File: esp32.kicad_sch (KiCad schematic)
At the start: 10 parts, among them U1 ESP32-C3-WROOM-02

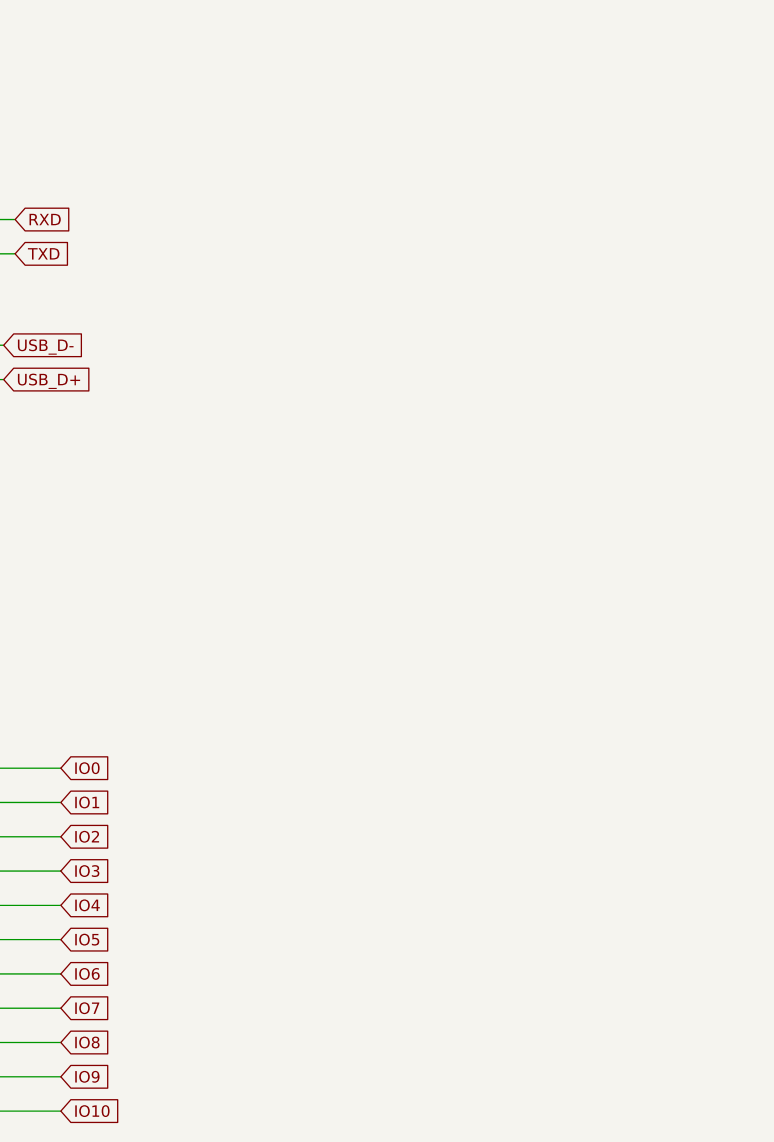
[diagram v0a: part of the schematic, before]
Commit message: Rework v4 schematic for Raspberry Pi 4/5 HAT
- Remap J1 to the Raspberry Pi 40-pin pinout (was still Orange Pi pin
  numbers: Pi 3V3 on MISO, GND on ESP32 RX)
- Fix auto-reset: U4 collectors drove EN and IO9 the wrong way round
- Let the Pi flash the ESP32: UART via 74LVC1G08 AND gate (U10) shared
  with the CP2102N, EN/BOOT on GPIO5/6 through 1k; add IO9 pull-up
- Power the Pi straight from +5V, drop the SS34 diode (D6)
- Add fan control: AO3400A low-side switch on GPIO18, tach on GPIO24
- Move mux LEDs D1-D3 off strapping pin GPIO8 to the 5V select lines
- Add 3V3 power LED and test points TP8-TP33
- Document v4 in CLAUDE.md

Co-Authored-By: Claude Opus 5.5 <noreply@anthropic.com>
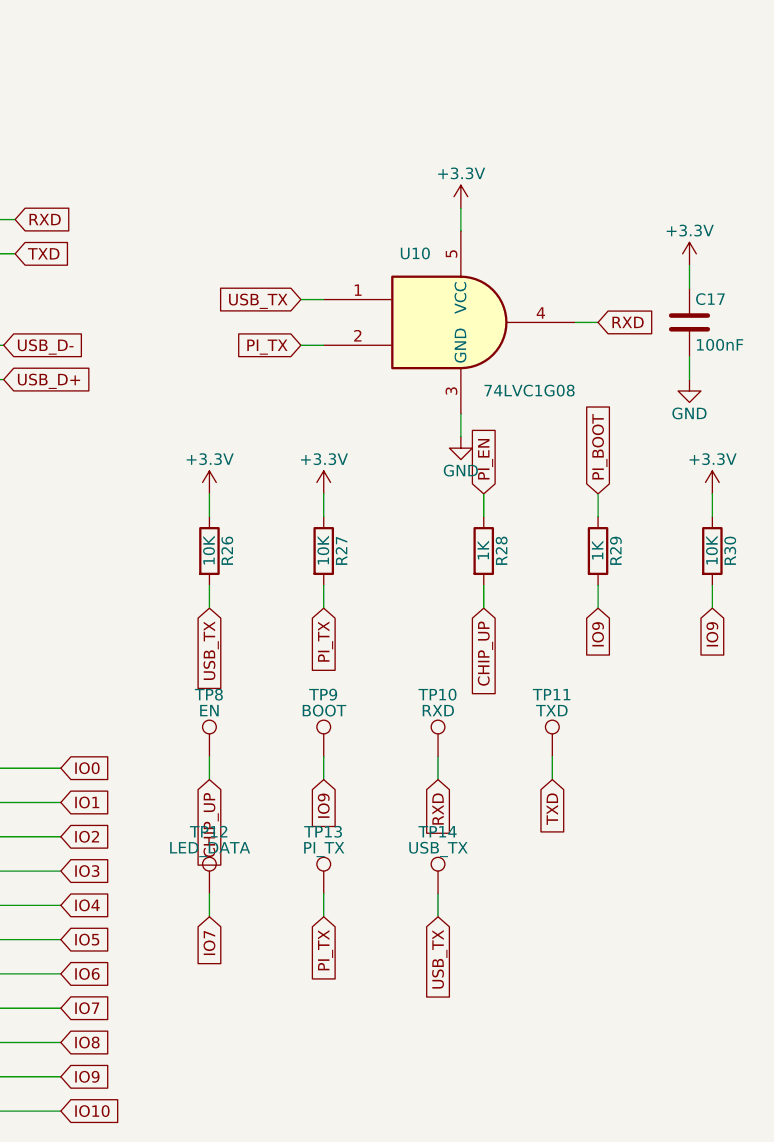
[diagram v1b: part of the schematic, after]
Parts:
- added C17: 100nF, Capacitor_SMD:C_0603_1608Metric, symbol Device:C
- added R26, R27, R30: 10K, Resistor_SMD:R_0603_1608Metric, symbol Device:R
- added R28, R29: 1K, Resistor_SMD:R_0603_1608Metric, symbol Device:R
- added TP10: RXD, TestPoint:TestPoint_Pad_1.0x1.0mm, symbol Connector:TestPoint
- added TP11: TXD, TestPoint:TestPoint_Pad_1.0x1.0mm, symbol Connector:TestPoint
- added TP12: LED_DATA, TestPoint:TestPoint_Pad_1.0x1.0mm, symbol Connector:TestPoint
- added TP13: PI_TX, TestPoint:TestPoint_Pad_1.0x1.0mm, symbol Connector:TestPoint
- added TP14: USB_TX, TestPoint:TestPoint_Pad_1.0x1.0mm, symbol Connector:TestPoint
- added TP8: EN, TestPoint:TestPoint_Pad_1.0x1.0mm, symbol Connector:TestPoint
- added TP9: BOOT, TestPoint:TestPoint_Pad_1.0x1.0mm, symbol Connector:TestPoint
- added U10: 74LVC1G08, Package_TO_SOT_SMD:SOT-353_SC-70-5, symbol 74xGxx:74LVC1G08
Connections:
- net +3.3V: now also C17.1, R26.1, R27.1, R30.1, U10.5 (VCC)
- net CHIP_UP: now also R28.2, TP8.1
- net GND: now also C17.2, U10.3 (GND)
- net IO7: now also TP12.1
- net IO9: now also R29.2, R30.2, TP9.1
- net RXD: now also TP10.1, U10.4
- net TXD: now also TP11.1
- new net PI_BOOT: R29.1
- new net PI_EN: R28.1
- new net PI_TX: R27.2, TP13.1, U10.2
- new net USB_TX: R26.2, TP14.1, U10.1

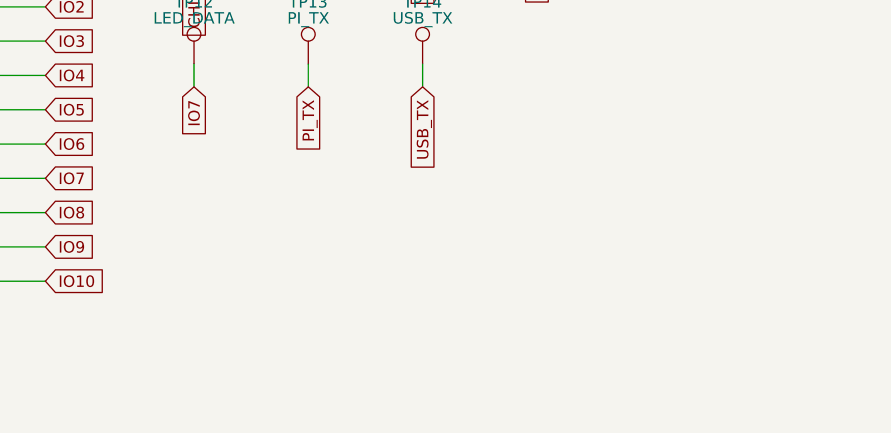
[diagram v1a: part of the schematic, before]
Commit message: Apply schematic review fixes, add JLCPCB rules, prepare for manual layout
Schematic (from a Codex review):
- R35 10k pull-up on GPIO2 (strapping pin; Pi MISO has a default pull-down)
- R36 10k pull-down on IO7 so the LEDs stay dark while the ESP32 boots
- C5 22uF for AMS1117 output stability, C7 1nF on GPIO9
- C18-C21 100nF decoupling for the level shifters U6-U9

Board:
- New parts parked outside the outline for manual placement
- Silkscreen scaled to JLCPCB's 1.0 mm minimum; back pinout table rebuilt
- C5/C7 values synced

Rules:
- JLCPCB 4-layer limits in Julelys.kicad_pro and new Julelys.kicad_dru

Co-Authored-By: Claude Opus 5.5 <noreply@anthropic.com>
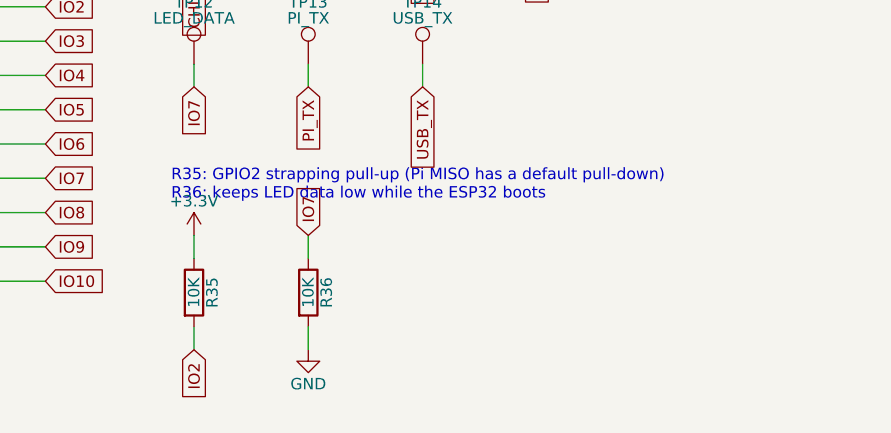
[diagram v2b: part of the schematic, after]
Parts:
- added R35, R36: 10K, Resistor_SMD:R_0603_1608Metric, symbol Device:R
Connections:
- net +3.3V: now also R35.1
- net GND: now also R36.2
- net IO2: now also R35.2
- net IO7: now also R36.1
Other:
- note added: "R35: GPIO2 strapping pull-up (Pi MISO has a default pull-down) R36: keeps LED data low while the ESP32 boots"
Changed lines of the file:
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@@
     )
   )
+  (symbol (lib_id "Device:R") (at 200.66 152.4 0) (unit 1)
+    (in_bom yes) (on_board yes) (dnp no)
+    (property "Reference" "R35" (at 202.692 152.4 90)
+      (effects (font (size 1.27 1.27)))
+    )
+    (property "Value" "10K" (at 200.66 152.4 90)
+      (effects (font (size 1.27 1.27)))
+    )
+    (property "Footprint" "Resistor_SMD:R_0603_1608Metric" (at 198.882 152.4 90)
+      (effects (font (size 1.27 1.27)) hide)
+    )
+    (property "Datasheet" "~" (at 200.66 152.4 0)
+      (effects (font (size 1.27 1.27)) hide)
+    )
+    (pin "1")
+    (pin "2")
+    (instances
+      (project "Julelys"
+        (path "/9ef41b73-8dcb-4021-8930-5b1db22eb182/9665c677-0b50-4f2a-bdc6-f5e1c3cc96ed"
+          (reference "R35") (unit 1)
+        )
+      )
+    )
+  )
+  (wire (pts (xy 200.66 148.59) (xy 200.66 146.05))
+    (stroke (width 0) (type default))
+  )
+  (symbol (lib_id "power:+3.3V") (at 200.66 146.05 0) (unit 1)
+    (in_bom yes) (on_board yes) (dnp no) (fields_autoplaced)
+    (property "Reference" "#PWR0201" (at 200.66 146.05 0)
+      (effects (font (size 1.27 1.27)) hide)
+    )
+    (property "Value" "+3.3V" (at 200.66 142.24 0)
+      (effects (font (size 1.27 1.27)))
+    )
+    (property "Footprint" "" (at 200.66 146.05 0)
+      (effects (font (size 1.27 1.27)) hide)
+    )
+    (property "Datasheet" "" (at 200.66 146.05 0)
+      (effects (font (size 1.27 1.27)) hide)
+    )
+    (pin "1")
+    (instances
+      (project "Julelys"
+        (path "/9ef41b73-8dcb-4021-8930-5b1db22eb182/9665c677-0b50-4f2a-bdc6-f5e1c3cc96ed"
+          (reference "#PWR0201") (unit 1)
+        )
+      )
+    )
+  )
+  (wire (pts (xy 200.66 156.21) (xy 200.66 158.75))
+    (stroke (width 0) (type default))
+  )
+  (global_label "IO2" (shape input) (at 200.66 158.75 270) (fields_autoplaced)
+    (effects (font (size 1.27 1.27)) (justify right))
+    (property "Intersheetrefs" "${INTERSHEET_REFS}" (at 200.66 158.75 270)
+      (effects (font (size 1.27 1.27)) (justify right) hide)
+    )
+  )
+  (symbol (lib_id "Device:R") (at 213.36 152.4 0) (unit 1)
+    (in_bom yes) (on_board yes) (dnp no)
+    (property "Reference" "R36" (at 215.392 152.4 90)
+      (effects (font (size 1.27 1.27)))
+    )
+    (property "Value" "10K" (at 213.36 152.4 90)
+      (effects (font (size 1.27 1.27)))
+    )
+    (property "Footprint" "Resistor_SMD:R_0603_1608Metric" (at 211.582 152.4 90)
+      (effects (font (size 1.27 1.27)) hide)
+    )
+    (property "Datasheet" "~" (at 213.36 152.4 0)
+      (effects (font (size 1.27 1.27)) hide)
+    )
+    (pin "1")
+    (pin "2")
+    (instances
+      (project "Julelys"
+        (path "/9ef41b73-8dcb-4021-8930-5b1db22eb182/9665c677-0b50-4f2a-bdc6-f5e1c3cc96ed"
+          (reference "R36") (unit 1)
+        )
+      )
+    )
+  )
+  (wire (pts (xy 213.36 148.59) (xy 213.36 146.05))
+    (stroke (width 0) (type default))
+  )
+  (global_label "IO7" (shape input) (at 213.36 146.05 90) (fields_autoplaced)
+    (effects (font (size 1.27 1.27)) (justify left))
+    (property "Intersheetrefs" "${INTERSHEET_REFS}" (at 213.36 146.05 90)
+      (effects (font (size 1.27 1.27)) (justify left) hide)
+    )
+  )
+  (wire (pts (xy 213.36 156.21) (xy 213.36 158.75))
+    (stroke (width 0) (type default))
+  )
+  (symbol (lib_id "power:GND") (at 213.36 158.75 0) (unit 1)
+    (in_bom yes) (on_board yes) (dnp no) (fields_autoplaced)
+    (property "Reference" "#PWR0202" (at 213.36 158.75 0)
+      (effects (font (size 1.27 1.27)) hide)
+    )
+    (property "Value" "GND" (at 213.36 162.56 0)
+      (effects (font (size 1.27 1.27)))
+    )
+    (property "Footprint" "" (at 213.36 158.75 0)
+      (effects (font (size 1.27 1.27)) hide)
+    )
+    (property "Datasheet" "" (at 213.36 158.75 0)
+      (effects (font (size 1.27 1.27)) hide)
+    )
+    (pin "1")
+    (instances
+      (project "Julelys"
+        (path "/9ef41b73-8dcb-4021-8930-5b1db22eb182/9665c677-0b50-4f2a-bdc6-f5e1c3cc96ed"
+          (reference "#PWR0202") (unit 1)
+        )
+      )
+    )
+  )
+  (text "R35: GPIO2 strapping pull-up (Pi MISO has a default pull-down)\nR36: keeps LED data low while the ESP32 boots" (at 198.12 142.24 0)
+    (effects (font (size 1.27 1.27)) (justify left bottom))
+  )
 )

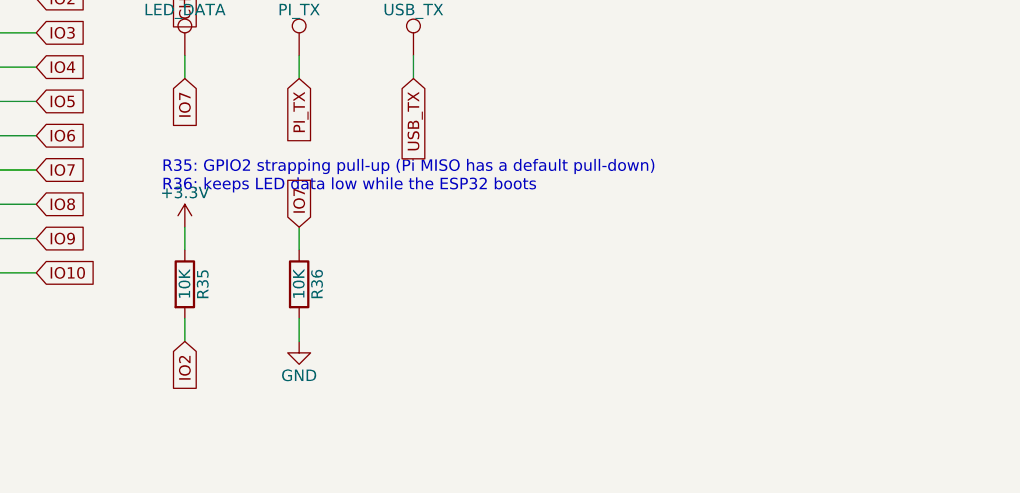
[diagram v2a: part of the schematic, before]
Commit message: Place decoupling caps, remove fan circuit and J3, add spare ESP32-Pi lines
Schematic:
- Remove the fan circuit (J13, Q1, D8, R31-R33, TP15-17); the Pi 5 drives
  its own Active Cooler. J1 pins 12/18 are now no-connect
- Remove the J3 debug header; J1 doubles as the dev header without a Pi
- IO0/IO1 to J1 pins 37/36 (Pi GPIO26/16) through R37/R38 1k as spare lines

Board:
- Test points moved to the bottom side to free space on top
- Decoupling caps C2/C3/C5/C8/C16/C18-C21 and R35/R36 placed next to
  their ICs; U8 nudged and R23/R10 moved to make room
- Conflicting tracks ripped up and rerouted; 6 connections left for
  interactive routing
- Back pinout table updated (fan and J3 rows replaced by J1 37/36)
- Courtyard exception rule for caps inside their IC's courtyard margin
- DRC (JLCPCB rules): 0 errors; ERC: 0 errors; schematic parity clean

Co-Authored-By: Claude Opus 5.5 <noreply@anthropic.com>
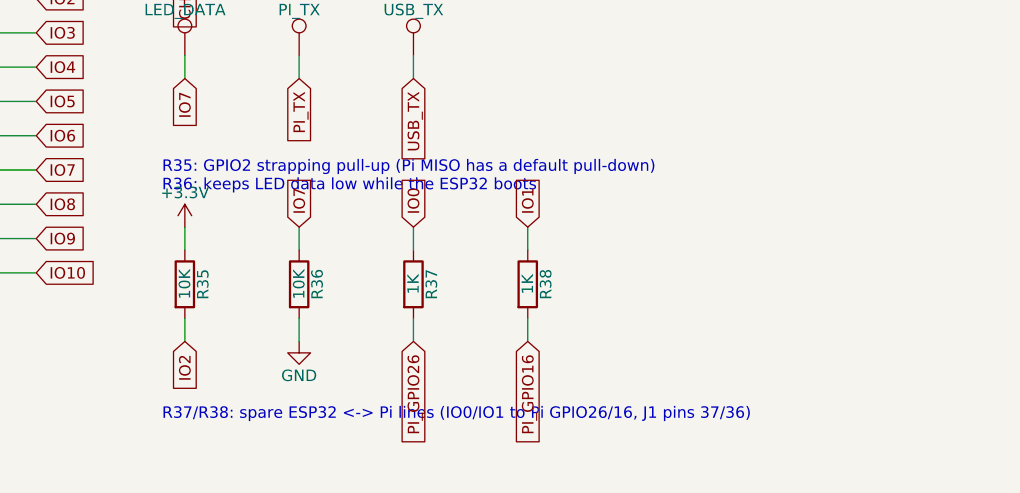
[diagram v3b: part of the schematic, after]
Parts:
- added R37, R38: 1K, Resistor_SMD:R_0603_1608Metric, symbol Device:R
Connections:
- net IO0: now also R37.1
- net IO1: now also R38.1
- new net PI_GPIO16: R38.2
- new net PI_GPIO26: R37.2
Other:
- note added: "R37/R38: spare ESP32 <-> Pi lines (IO0/IO1 to Pi GPIO26/16, J1 pins 37/36)"
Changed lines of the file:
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@@
+    (effects (font (size 1.27 1.27)) (justify left bottom))
+  )
+  (symbol (lib_id "Device:R") (at 226.06 152.4 0) (unit 1)
+    (in_bom yes) (on_board yes) (dnp no)
+    (property "Reference" "R37" (at 228.092 152.4 90)
+      (effects (font (size 1.27 1.27)))
+    )
+    (property "Value" "1K" (at 226.06 152.4 90)
+      (effects (font (size 1.27 1.27)))
+    )
+    (property "Footprint" "Resistor_SMD:R_0603_1608Metric" (at 224.282 152.4 90)
+      (effects (font (size 1.27 1.27)) hide)
+    )
+    (property "Datasheet" "~" (at 226.06 152.4 0)
+      (effects (font (size 1.27 1.27)) hide)
+    )
+    (pin "1")
+    (pin "2")
+    (instances
+      (project "Julelys"
+        (path "/9ef41b73-8dcb-4021-8930-5b1db22eb182/9665c677-0b50-4f2a-bdc6-f5e1c3cc96ed"
+          (reference "R37") (unit 1)
+        )
+      )
+    )
+  )
+  (wire (pts (xy 226.06 148.59) (xy 226.06 146.05))
+    (stroke (width 0) (type default))
+  )
+  (global_label "IO0" (shape input) (at 226.06 146.05 90) (fields_autoplaced)
+    (effects (font (size 1.27 1.27)) (justify left))
+    (property "Intersheetrefs" "${INTERSHEET_REFS}" (at 226.06 146.05 90)
+      (effects (font (size 1.27 1.27)) (justify left) hide)
+    )
+  )
+  (wire (pts (xy 226.06 156.21) (xy 226.06 158.75))
+    (stroke (width 0) (type default))
+  )
+  (global_label "PI_GPIO26" (shape input) (at 226.06 158.75 270) (fields_autoplaced)
+    (effects (font (size 1.27 1.27)) (justify right))
+    (property "Intersheetrefs" "${INTERSHEET_REFS}" (at 226.06 158.75 270)
+      (effects (font (size 1.27 1.27)) (justify right) hide)
+    )
+  )
+  (symbol (lib_id "Device:R") (at 238.76 152.4 0) (unit 1)
+    (in_bom yes) (on_board yes) (dnp no)
+    (property "Reference" "R38" (at 240.792 152.4 90)
+      (effects (font (size 1.27 1.27)))
+    )
+    (property "Value" "1K" (at 238.76 152.4 90)
+      (effects (font (size 1.27 1.27)))
+    )
+    (property "Footprint" "Resistor_SMD:R_0603_1608Metric" (at 236.982 152.4 90)
+      (effects (font (size 1.27 1.27)) hide)
+    )
+    (property "Datasheet" "~" (at 238.76 152.4 0)
+      (effects (font (size 1.27 1.27)) hide)
+    )
+    (pin "1")
+    (pin "2")
+    (instances
+      (project "Julelys"
+        (path "/9ef41b73-8dcb-4021-8930-5b1db22eb182/9665c677-0b50-4f2a-bdc6-f5e1c3cc96ed"
+          (reference "R38") (unit 1)
+        )
+      )
+    )
+  )
+  (wire (pts (xy 238.76 148.59) (xy 238.76 146.05))
+    (stroke (width 0) (type default))
+  )
+  (global_label "IO1" (shape input) (at 238.76 146.05 90) (fields_autoplaced)
+    (effects (font (size 1.27 1.27)) (justify left))
+    (property "Intersheetrefs" "${INTERSHEET_REFS}" (at 238.76 146.05 90)
+      (effects (font (size 1.27 1.27)) (justify left) hide)
+    )
+  )
+  (wire (pts (xy 238.76 156.21) (xy 238.76 158.75))
+    (stroke (width 0) (type default))
+  )
+  (global_label "PI_GPIO16" (shape input) (at 238.76 158.75 270) (fields_autoplaced)
+    (effects (font (size 1.27 1.27)) (justify right))
+    (property "Intersheetrefs" "${INTERSHEET_REFS}" (at 238.76 158.75 270)
+      (effects (font (size 1.27 1.27)) (justify right) hide)
+    )
+  )
+  (text "R37/R38: spare ESP32 <-> Pi lines (IO0/IO1 to Pi GPIO26/16, J1 pins 37/36)" (at 198.12 167.64 0)
     (effects (font (size 1.27 1.27)) (justify left bottom))
   )
